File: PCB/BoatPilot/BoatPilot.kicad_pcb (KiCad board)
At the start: 4 copper layers, 65 x 35.5 mm, 107 parts, among them J101 battery, J102 Raspberry_Pi_2_3, J103 FlexInput, J104 out 1, J105 SWD, J106 out 2, J107 out 3, J108 UART, J109 out 4, J110 out 5, J111 out 6, J112 GPS, J113 I2C Flex, J114 wind, J115 ANT, J116 USB_OTG, J117 Micro_SD_Card, Q101 TSM3457, U101 TPS565208, U102 TLV75733PDBV, U103 TLV75733PDBV, U104 BMX160, U105 STM32F405RGTx, U106 74LVC1G86, U107 BMP280, U108 W25Q128JVS, U109 TLV75733PDBV, U111 RFM69HCW, Y101 8MHz

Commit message: Working on the layout
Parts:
- added R101: 10k, Resistor_SMD:R_0603_1608Metric, F.Cu at (30.3, 52.9)
- R119: moved to F.Cu
- U107: value BMP280 -> P-SENSE; footprint Package_LGA:Bosch_LGA-8_2x2.5mm_P0.65mm_ClockwisePinNumbering -> Package_SO:SOIC-8_3.9x4.9mm_P1.27mm
- moved C125 17.2 mm to (31.0, 49.7)
- moved R118 15.2 mm to (31.8, 47.5), turned to 0 degrees
- moved U107 14.8 mm to (35.5, 51.0), turned to 0 degrees
- moved R119 11.1 mm to (34.8, 47.5), turned to 0 degrees
- moved R112 9.94 mm to (48.9, 51.8), turned to 270 degrees
- moved R110 6.23 mm to (50.8, 46.7)
- moved C117 2.52 mm to (42.0, 51.8)
- moved C118 2.52 mm to (47.4, 51.8)
- moved R111 2.52 mm to (40.5, 51.8)
- moved U104 2.52 mm to (44.7, 51.9)
- moved R134 1.09 mm to (27.5, 49.7)
- moved R130 0.99 mm to (29.5, 49.7)
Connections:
- U105 pad 20: /~CS_BMX160 -> /~CS_BMP280
- U105 pad 24: /~CS_SDCARD -> /~CS_BMX160
- U105 pad 59: /~CS_BMP280 -> /~CS_SDCARD
- U107 pad 1: GND -> Net-(C125-Pad2)
- U107 pad 2: /~CS_BMP280 -> GND
- U107 pad 3: /SPI1_MOSI -> (no net)
- U107 pad 4: /SPI1_SCK -> Net-(R101-Pad2)
- U107 pad 5: /SPI1_MISO -> /~CS_BMP280
- U107 pad 6: Net-(C125-Pad2) -> /SPI1_SCK
- U107 pad 7: GND -> /SPI1_MOSI
- U107 pad 8: Net-(C125-Pad2) -> /SPI1_MISO
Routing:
- net /~CS_BMP280: track 0.00 -> 15.4 mm
- net Net-(C117-Pad2): track 0.00 -> 11.9 mm, vias 0 -> 3
- net /SPI1_SCK: track 0.00 -> 11.7 mm
- net Net-(C122-Pad2): track 0.00 -> 9.22 mm
- net Net-(C123-Pad2): track 0.00 -> 8.93 mm
- net +3.3VA: track 42.5 -> 33.8 mm, vias 7 -> 5
- net /SPI1_MOSI: track 0.00 -> 7.70 mm
- net /SPI1_MISO: track 0.00 -> 7.32 mm
- net Net-(JP101-Pad2): track 0.00 -> 5.72 mm, vias 0 -> 1
- net Net-(C116-Pad2): track 0.00 -> 4.79 mm, vias 0 -> 1
- net GND: track 16.9 -> 21.4 mm, vias 26 -> 32
- net Net-(C125-Pad2): track 0.00 -> 3.60 mm
- net /~RST: track 0.00 -> 3.05 mm
- net /SPI2_CS: track 15.1 -> 12.3 mm
- net Net-(R101-Pad2): track 0.00 -> 1.98 mm
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
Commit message: Routing in work
nightly commit
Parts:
- removed R120: 10k, Resistor_SMD:R_0603_1608Metric
- turned RN101 to 90 degrees
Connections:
- net Net-(C131-Pad2) renamed /RFM_SUP
- J102 pad 11: Net-(J102-Pad11) -> (no net)
- J102 pad 12: Net-(J102-Pad12) -> (no net)
- J102 pad 13: Net-(J102-Pad13) -> (no net)
- J102 pad 16: Net-(J102-Pad16) -> (no net)
- J102 pad 18: Net-(J102-Pad18) -> (no net)
- J102 pad 22: Net-(J102-Pad22) -> (no net)
- J102 pad 26: Net-(J102-Pad26) -> (no net)
- J102 pad 27: Net-(J102-Pad27) -> (no net)
- J102 pad 28: Net-(J102-Pad28) -> (no net)
- J102 pad 29: Net-(J102-Pad29) -> (no net)
- J102 pad 31: Net-(J102-Pad31) -> (no net)
- J102 pad 32: Net-(J102-Pad32) -> (no net)
- J102 pad 33: Net-(J102-Pad33) -> (no net)
- J102 pad 35: Net-(J102-Pad35) -> (no net)
- J102 pad 36: Net-(J102-Pad36) -> (no net)
- J102 pad 37: Net-(J102-Pad37) -> (no net)
- J102 pad 38: Net-(J102-Pad38) -> (no net)
- J102 pad 40: Net-(J102-Pad40) -> (no net)
- J102 pad 7: Net-(J102-Pad7) -> (no net)
- J105 pad 2: /SYS_SWDIO -> /SYS_SWCLK
- J105 pad 3: /SYS_SWCLK -> /SYS_SWDIO
- J105 pad 5: Net-(J105-Pad5) -> (no net)
- J112 pad 2: /UART2_TX -> (no net)
- J112 pad 3: /UART2_RX -> (no net)
- J116 pad 4: Net-(J116-Pad4) -> (no net)
- J117 pad 1: Net-(J117-Pad1) -> (no net)
- J117 pad 8: Net-(J117-Pad8) -> (no net)
- RN101 pad 1: /~CS_SDCARD -> /SPI3_MISO
- RN101 pad 2: /SPI3_MOSI -> /SPI3_SCK
- RN101 pad 3: /SPI3_SCK -> /SPI3_MOSI
- RN101 pad 4: /SPI3_MISO -> /~CS_SDCARD
- U105 pad 11: Net-(R120-Pad2) -> (no net)
- U105 pad 14: /SERVO_OUT6 -> /SERVO_OUT3
- U105 pad 15: /SERVO_OUT5 -> /SERVO_OUT4
- U105 pad 16: /SERVO_OUT4 -> /SERVO_OUT5
- U105 pad 17: /SERVO_OUT3 -> /SERVO_OUT6
- U105 pad 2: Net-(U105-Pad2) -> (no net)
- U105 pad 25: /VBUS_SENSE -> /BMX160_INT1
- U105 pad 54: /~RFM69_IRQ -> /~CS_SDCARD
- U105 pad 56: /BMX160_INT1 -> /VBUS_SENSE
- U105 pad 59: /~CS_SDCARD -> /~RFM69_IRQ
- U111 pad 11: Net-(U111-Pad11) -> (no net)
- U111 pad 12: Net-(U111-Pad12) -> (no net)
- U111 pad 15: Net-(U111-Pad15) -> (no net)
- U111 pad 16: Net-(U111-Pad16) -> (no net)
- U111 pad 7: Net-(U111-Pad7) -> (no net)
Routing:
- net +3.3VP: track 0.00 -> 64.2 mm, vias 0 -> 2
- net /I2C1_SDA: track 0.00 -> 51.7 mm, vias 1 -> 2
- net /I2C1_SCL: track 0.00 -> 51.3 mm, vias 1 -> 2
- net /WIND_PWM: track 0.00 -> 44.2 mm, vias 0 -> 2
- net /SPI3_MISO: track 0.00 -> 40.3 mm, vias 0 -> 3
- net /UART6_RX: track 20.4 -> 56.7 mm, vias 0 -> 2
- net /SERVO_OUT1: track 0.00 -> 35.3 mm, vias 0 -> 2
- net /SERVO_OUT2: track 0.00 -> 34.6 mm, vias 0 -> 2
- net /SPI3_MOSI: track 0.00 -> 34.5 mm, vias 0 -> 4
- net /UART6_TX: track 18.5 -> 52.8 mm, vias 0 -> 2
- net /SPI3_SCK: track 0.00 -> 32.6 mm, vias 0 -> 4
- net /~CS_SDCARD: track 0.00 -> 30.3 mm, vias 0 -> 3
- net /SERVO_OUT3: track 0.00 -> 22.6 mm
- net /~RST: track 3.05 -> 25.1 mm, vias 0 -> 3
- net /I2C2_SCL: track 0.00 -> 21.6 mm, vias 1 -> 2
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
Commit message: Layout in work
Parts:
- moved D101 7.56 mm to (36.1, 35.4), turned to 90 degrees
- moved D102 5.55 mm to (37.6, 35.4), turned to 90 degrees
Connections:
- U105 pad 11: (no net) -> /RFM_RST
- U105 pad 3: /LED_WARN -> /LED_STAT
- U105 pad 4: /LED_STAT -> /LED_WARN
- U105 pad 57: /BMX160_INT2 -> /UART_INV
- U105 pad 58: /RFM_RST -> /BMX160_INT2
- U105 pad 8: /UART_INV -> (no net)
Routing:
- net +5V: track 20.7 -> 106.1 mm, vias 0 -> 10
- net /UART_INV: track 3.22 -> 48.2 mm, vias 0 -> 3
- net +3.3VA: track 20.6 -> 65.3 mm
- net /SPI3_SCK: track 32.6 -> 71.8 mm
- net /UBATT: track 1.47 -> 35.4 mm, vias 0 -> 1
- net /SPI3_MOSI: track 34.5 -> 66.9 mm
- net /~CS_RFM69: track 1.58 -> 32.8 mm, vias 1 -> 4
- net /VBUS_SENSE: track 1.89 -> 27.9 mm, vias 0 -> 1
- net /SPI3_MISO: track 40.3 -> 62.2 mm
- net Net-(J102-Pad15): track 0.00 -> 21.9 mm, vias 0 -> 2
- net /RFM_RST: track 1.56 -> 19.1 mm, vias 1 -> 2
- net /BMX160_INT2: track 0.00 -> 17.3 mm, vias 0 -> 2
- net +3V3: track 34.9 -> 44.4 mm, vias 31 -> 36
- net Net-(D101-Pad2): track 1.47 -> 8.15 mm
- net /LED_WARN: track 0.00 -> 5.17 mm
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- added copper zone on B.Cu, net +3V3
- added copper zone on F.Cu, net +3V3

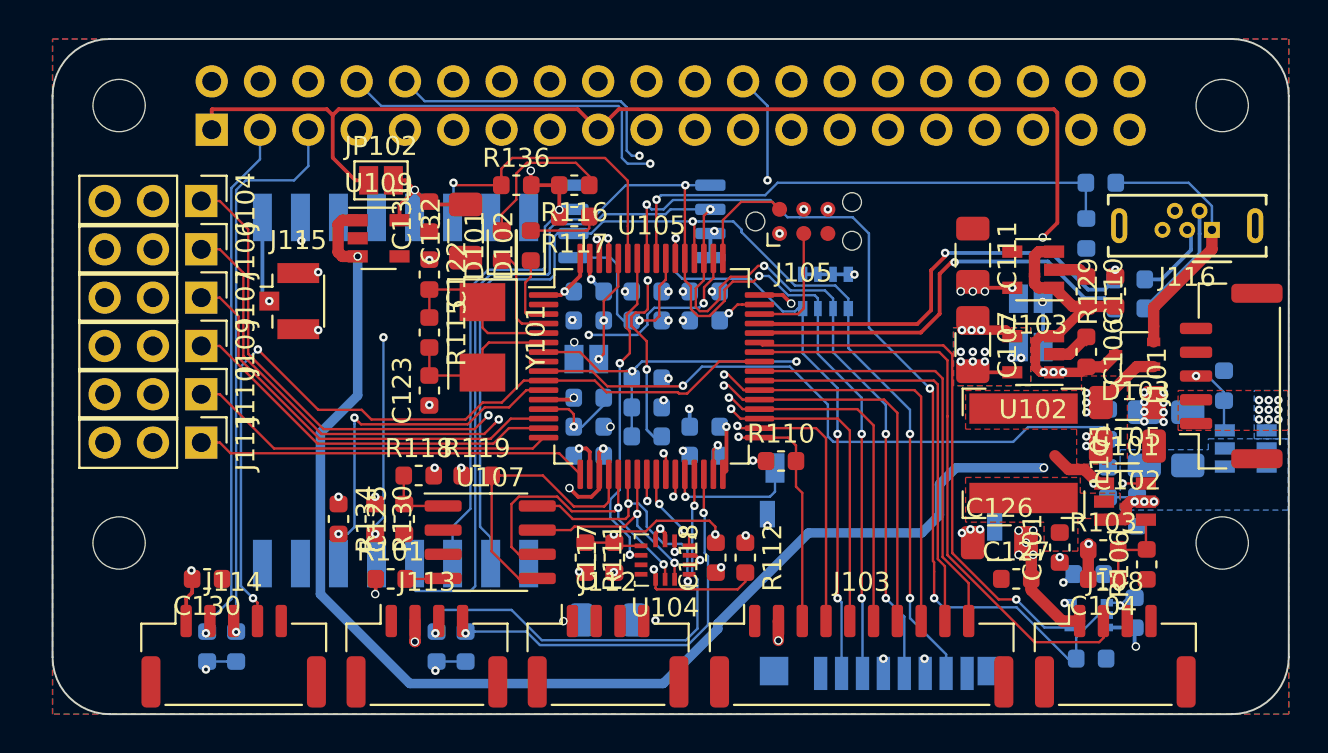
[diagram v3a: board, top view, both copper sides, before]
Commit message: Add DMC code and clean layout
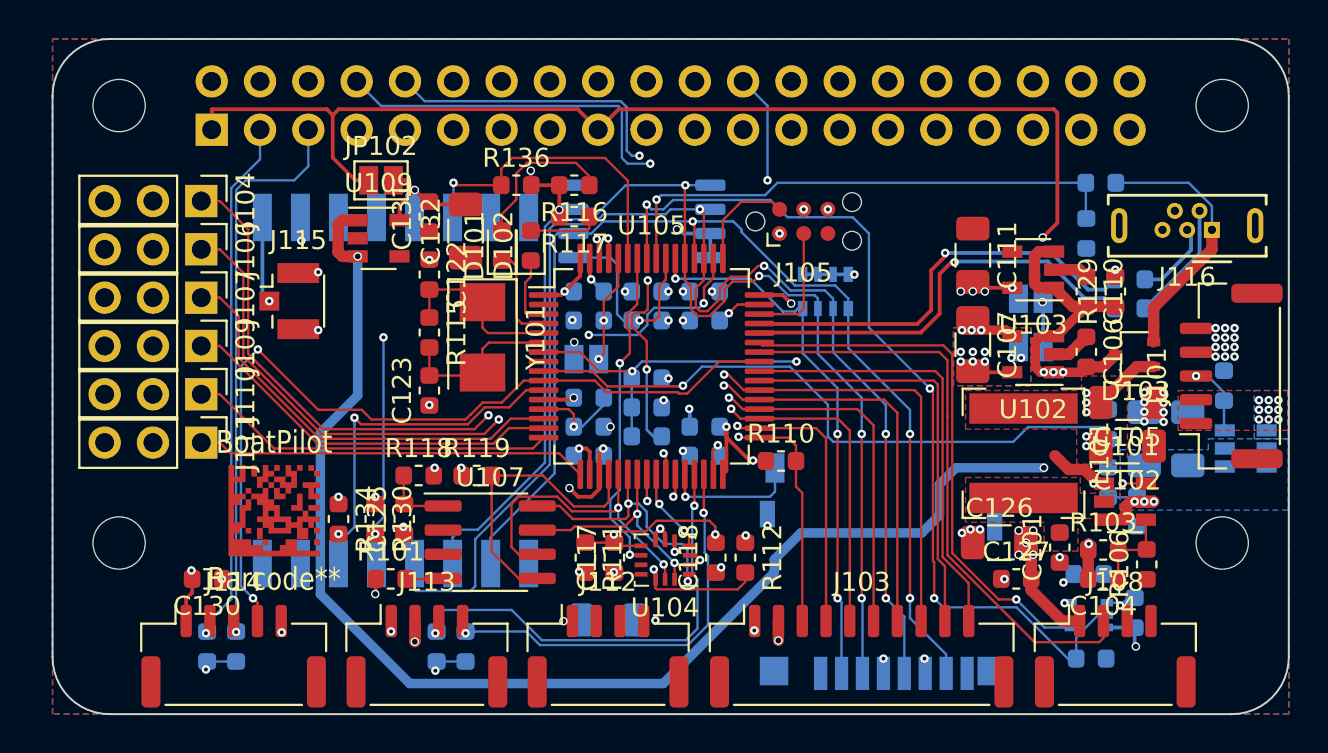
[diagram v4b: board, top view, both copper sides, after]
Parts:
- added Barcode**: BoatPilot, footprint:BoatPilot, F.Cu at (24.1, 49.3)
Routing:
- net +3V3: track 44.4 -> 49.2 mm
- net /SPI3_MISO: track 62.2 -> 59.9 mm
- net /~CS_SDCARD: track 30.5 -> 28.6 mm
- net /SPI3_SCK: track 71.8 -> 70.0 mm
- net /SPI3_MOSI: track 66.9 -> 65.7 mm
- net /SPI2_SCK: track 30.2 -> 30.8 mm
- net GND: vias 39 -> 57

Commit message: Further layout work
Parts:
- added D104: LED, LED_SMD:LED_0603_1608Metric, F.Cu at (30.4, 42.9)
- added FID101: Fiducial, Fiducial:Fiducial_0.75mm_Mask1.5mm, F.Cu at (14.9, 57.7)
- added FID102: Fiducial, Fiducial:Fiducial_0.75mm_Mask1.5mm, B.Cu at (74.8, 57.5)
- added FID103: Fiducial, Fiducial:Fiducial_0.75mm_Mask1.5mm, F.Cu at (70.8, 30.8)
- added P101: ICT-Point, TestPoint:TestPoint_Pad_D1.0mm, F.Cu at (57.6, 36.1)
- added P102: ICT-Point, TestPoint:TestPoint_Pad_D1.0mm, B.Cu at (46.7, 43.1)
- added P104: ICT-Point, TestPoint:TestPoint_Pad_D1.0mm, F.Cu at (57.6, 38.3)
- added P105: ICT-Point, TestPoint:TestPoint_Pad_D1.0mm, F.Cu at (28.5, 37.9)
- added P106: ICT-Point, TestPoint:TestPoint_Pad_D1.0mm, B.Cu at (41.6, 51.6)
- added P107: ICT-Point, TestPoint:TestPoint_Pad_D1.0mm, F.Cu at (60.9, 32.6)
- added P108: ICT-Point, TestPoint:TestPoint_Pad_D1.0mm, B.Cu at (58.2, 34.5)
- added P109: ICT-Point, TestPoint:TestPoint_Pad_D1.0mm, B.Cu at (76.0, 40.7)
- added P110: ICT-Point, TestPoint:TestPoint_Pad_D1.0mm, F.Cu at (20.1, 49.0)
- added P111: ICT-Point, TestPoint:TestPoint_Pad_D1.0mm, B.Cu at (45.6, 40.8)
- added P112: ICT-Point, TestPoint:TestPoint_Pad_D1.0mm, F.Cu at (26.0, 33.2)
- added R107: 2.2k, Resistor_SMD:R_0603_1608Metric, F.Cu at (30.4, 39.9)
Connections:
- U105 pad 8: (no net) -> Net-(D104-Pad1)
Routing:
- net Net-(D104-Pad1): track 0.00 -> 8.87 mm, vias 0 -> 2
- net /RFM_SUP: track 7.69 -> 13.2 mm
- net +3.3VA: track 65.3 -> 67.3 mm, vias 7 -> 8
- net Net-(D104-Pad2): track 0.00 -> 1.47 mm
- net /UBATT: track 35.4 -> 36.6 mm
- net /~RST: track 25.1 -> 25.7 mm
- net +3V3: vias 36 -> 38

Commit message: Layout cleanup
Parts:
- removed R108: 0R, Resistor_SMD:R_0603_1608Metric
- added C133: 10u, Capacitor_SMD:C_0805_2012Metric, B.Cu at (74.0, 36.7)
- added JP105: RST, Jumper:SolderJumper-2_P1.3mm_Open_Pad1.0x1.5mm, B.Cu at (43.6, 46.3)
- C102, C103, C105, C107, C108, C111, C126, C128, C132: footprint Capacitor_SMD:C_1206_3216Metric -> Capacitor_SMD:C_0805_2012Metric
- C104: value nb -> 10n
- J117: footprint Connector_Card:microSD_HC_Hirose_DM3D-SF -> SilentWorks:AMPHENOL_1140084168
- R109, R111, R118: footprint Resistor_SMD:R_0603_1608Metric -> Inductor_SMD:L_0603_1608Metric
- R113: value 4.7k -> 10k
- RN101: footprint Resistor_SMD:R_Array_Convex_4x0603 -> Resistor_SMD:R_Cat16-4
- U111: value RFM69HCW -> RFM69HW
- moved J117 5.48 mm to (55.1, 57.9)
- moved P108 1.31 mm to (57.1, 33.8)
- moved C102 0.44 mm to (69.0, 45.5)
- moved C108 0.27 mm to (70.1, 45.7)
- moved C103 0.19 mm to (72.2, 45.7)
- moved C105 0.13 mm to (69.0, 43.5)
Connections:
- net /VBUS renamed VBUS
- J102 pad 11: (no net) -> Net-(J102-Pad11)
- J102 pad 12: (no net) -> Net-(J102-Pad12)
- J102 pad 13: (no net) -> Net-(J102-Pad13)
- J102 pad 16: (no net) -> Net-(J102-Pad16)
- J102 pad 18: (no net) -> Net-(J102-Pad18)
- J102 pad 22: (no net) -> Net-(J102-Pad22)
- J102 pad 26: (no net) -> Net-(J102-Pad26)
- J102 pad 27: (no net) -> Net-(J102-Pad27)
- J102 pad 28: (no net) -> Net-(J102-Pad28)
- J102 pad 29: (no net) -> Net-(J102-Pad29)
- J102 pad 31: (no net) -> Net-(J102-Pad31)
- J102 pad 32: (no net) -> Net-(J102-Pad32)
- J102 pad 33: (no net) -> Net-(J102-Pad33)
- J102 pad 35: (no net) -> Net-(J102-Pad35)
- J102 pad 36: (no net) -> Net-(J102-Pad36)
- J102 pad 37: (no net) -> Net-(J102-Pad37)
- J102 pad 38: (no net) -> Net-(J102-Pad38)
- J102 pad 40: (no net) -> Net-(J102-Pad40)
- J102 pad 7: (no net) -> Net-(J102-Pad7)
- J105 pad 5: (no net) -> Net-(J105-Pad5)
- J112 pad 2: (no net) -> /UART2_TX
- J112 pad 3: (no net) -> /UART2_RX
- J116 pad 4: (no net) -> Net-(J116-Pad4)
- J117 pad 1: (no net) -> Net-(J117-Pad1)
- J117 pad 10: /CARD_DET -> GND
- J117 pad 8: (no net) -> Net-(J117-Pad8)
- J117 pad 9: GND -> /CARD_DET
- U105 pad 2: (no net) -> Net-(U105-Pad2)
- U111 pad 11: (no net) -> Net-(U111-Pad11)
- U111 pad 12: (no net) -> Net-(U111-Pad12)
- U111 pad 15: (no net) -> Net-(U111-Pad15)
- U111 pad 16: (no net) -> Net-(U111-Pad16)
- U111 pad 7: (no net) -> Net-(U111-Pad7)
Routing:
- net /UART_INV: track 48.2 -> 52.5 mm
- net +5V: track 106.4 -> 102.3 mm
- net GND: track 25.0 -> 28.9 mm, vias 57 -> 56
- net /~RST: track 25.7 -> 28.4 mm
- net /CARD_DET: track 7.26 -> 5.20 mm
- net VBUS: track 14.0 -> 16.0 mm
- net +3V3: track 49.2 -> 50.9 mm
- net +BATT: track 57.1 -> 58.7 mm
- net /I2C2_SDA: track 22.0 -> 20.8 mm
- net /I2C2_SCL: track 24.0 -> 22.8 mm
- net /SPI3_MISO: track 59.9 -> 61.1 mm
- net /UBATT: track 36.6 -> 37.7 mm
- net Net-(J102-Pad15): track 21.6 -> 20.6 mm
- net /SPI3_SCK: track 70.0 -> 70.8 mm
- net /SPI3_MOSI: track 65.7 -> 66.4 mm
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- added copper zone on B.Cu, net +5V
- added copper zone on F.Cu, net +5V
- added copper zone on In2.Cu, net +5V

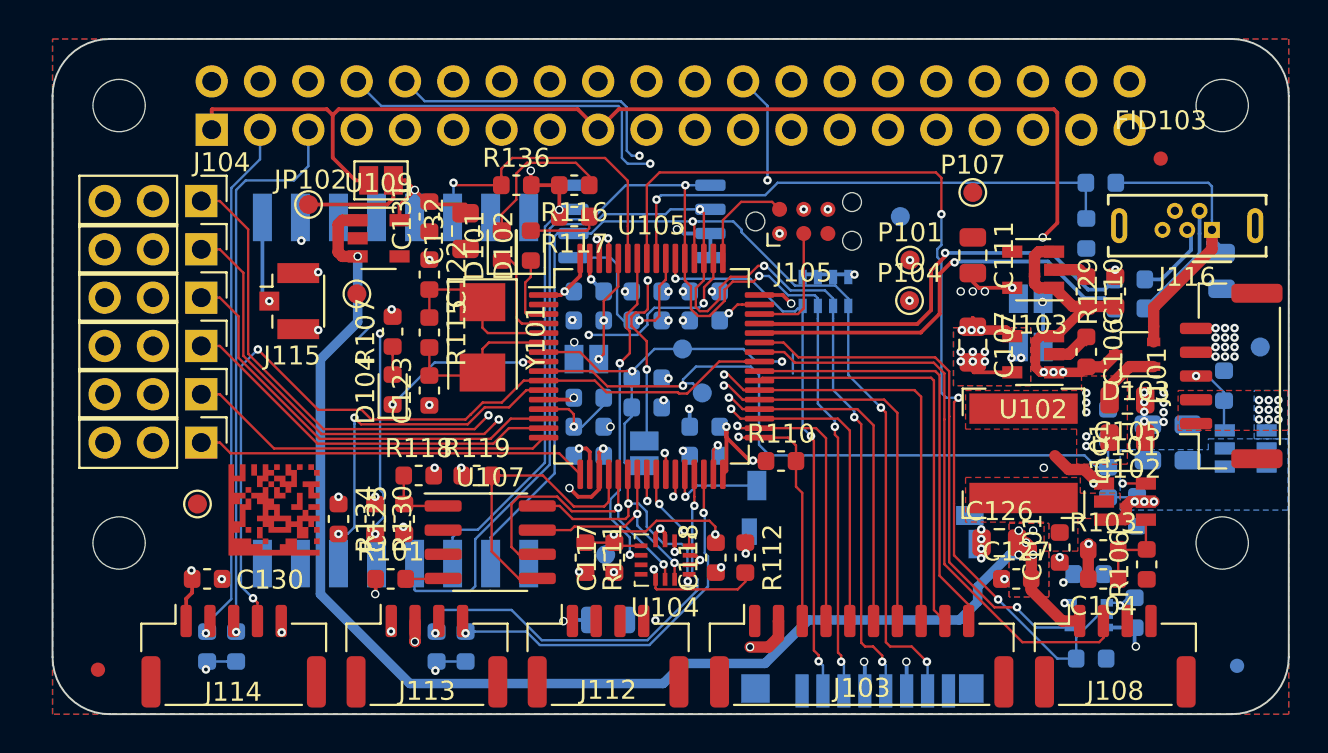
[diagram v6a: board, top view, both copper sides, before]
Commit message: Layout review and cleanup, silkscreen cleanup
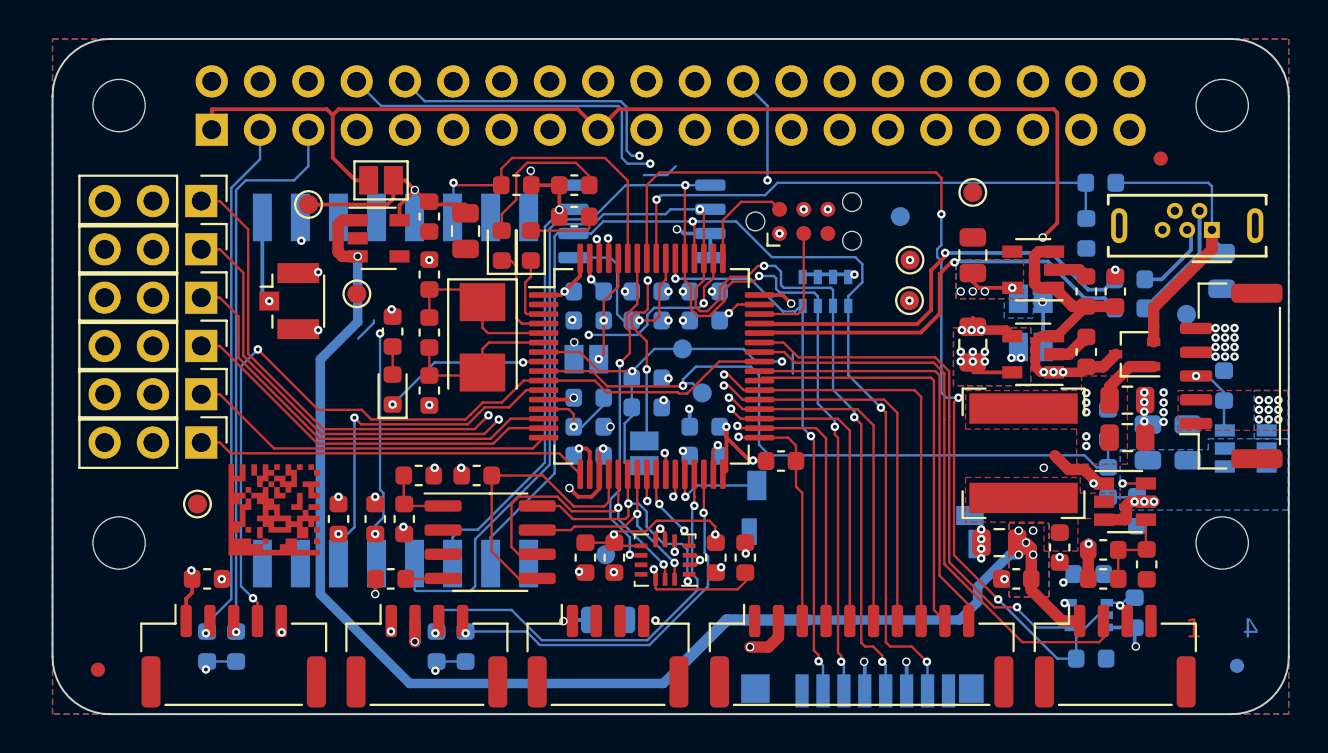
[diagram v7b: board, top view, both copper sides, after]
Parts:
- moved P109 4.24 mm to (72.1, 39.0)
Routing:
- net /SPI3_MISO: track 61.1 -> 63.0 mm
- net GND: track 28.9 -> 30.8 mm
- net /SPI3_SCK: track 70.8 -> 71.5 mm
- added copper zone on B.Cu, net +3.3VA
- added copper zone on F.Cu, net +3.3VA
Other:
- board text added: "1"
- board text added: "2"
- board text added: "3"
- board text added: "4"
- board text added: "JLCJLCJLCJLC"
